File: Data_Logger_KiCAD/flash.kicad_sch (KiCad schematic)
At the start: 1 part, among them U2 W25Q128JVS

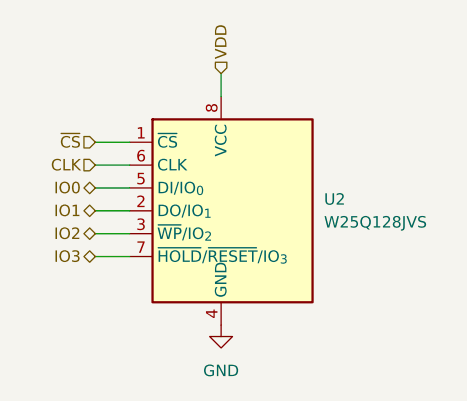
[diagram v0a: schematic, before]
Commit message: Aggregated sub schematics into single primary schematic
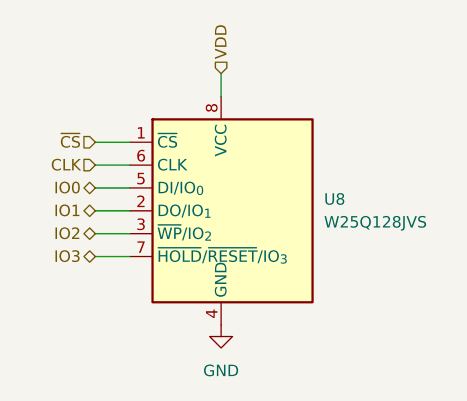
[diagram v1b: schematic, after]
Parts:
- renumbered U2 to U8
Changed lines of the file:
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@@
 		(dnp no)
 		(fields_autoplaced yes)
-		(property "Reference" "#PWR?"
+		(property "Reference" "#PWR045"
 			(at 120.65 91.44 0)
 			(effects
@@
 			(project "Data_Logger_Board"
 				(path "/db968e42-3ace-4cc9-9096-9d8f48135c40/795ab2be-9db7-4254-b05c-ac2b60177344/acf294b8-d265-4db4-b17e-5e21ef63ae9d"
-					(reference "#PWR?")
+					(reference "#PWR045")
 					(unit 1)
 				)
@@
 		(dnp no)
 		(fields_autoplaced yes)
-		(property "Reference" "U?"
+		(property "Reference" "U8"
 			(at 132.08 71.1199 0)
 			(effects
@@
 			(project "Data_Logger_Board"
 				(path "/db968e42-3ace-4cc9-9096-9d8f48135c40/795ab2be-9db7-4254-b05c-ac2b60177344/acf294b8-d265-4db4-b17e-5e21ef63ae9d"
-					(reference "U?")
+					(reference "U8")
 					(unit 1)
 				)
